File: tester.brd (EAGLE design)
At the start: 56 x 67 mm, 71 parts, among them IC1 ATmega8/88/168, K1 NA 05W K, M1 SP6000C-180, P1 250, P2 10k lin, Q1 BC847CSMD, Q2 BC847CSMD, Q3 BC807-40SMD, Q4 8,000 MHz, Q5 BC847CSMD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

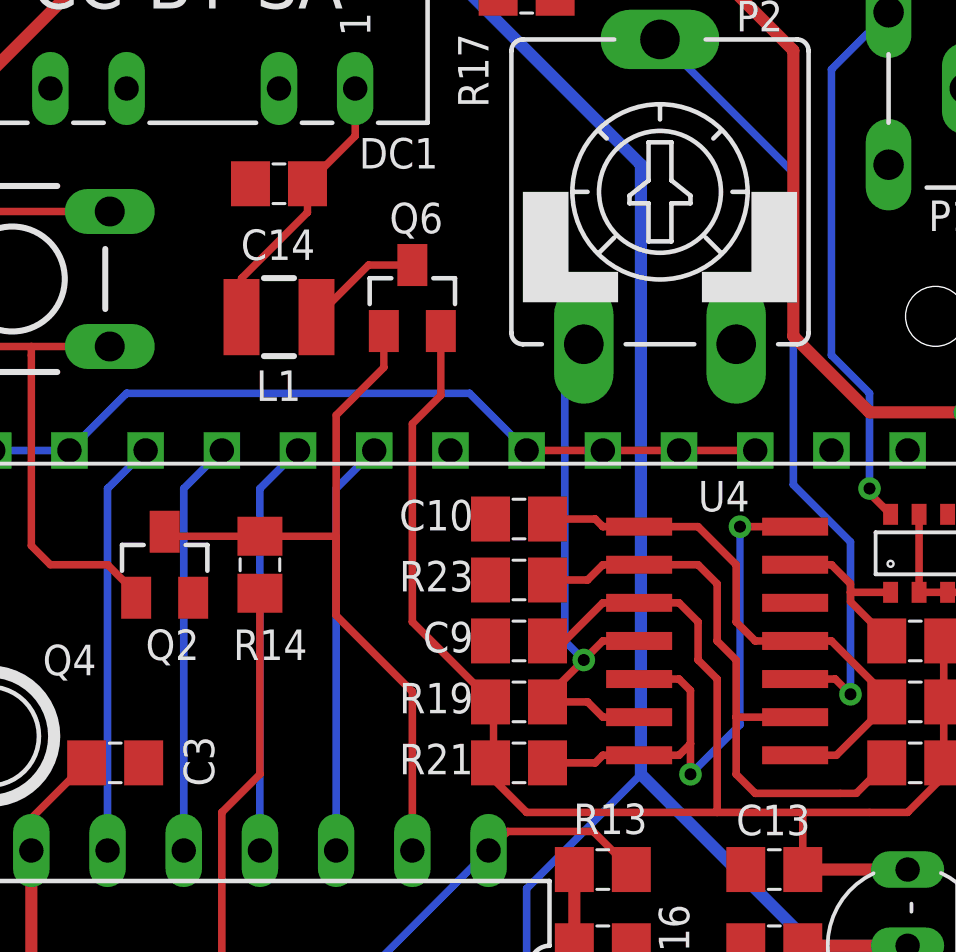
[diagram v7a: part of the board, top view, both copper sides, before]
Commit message: bigger pads for L1
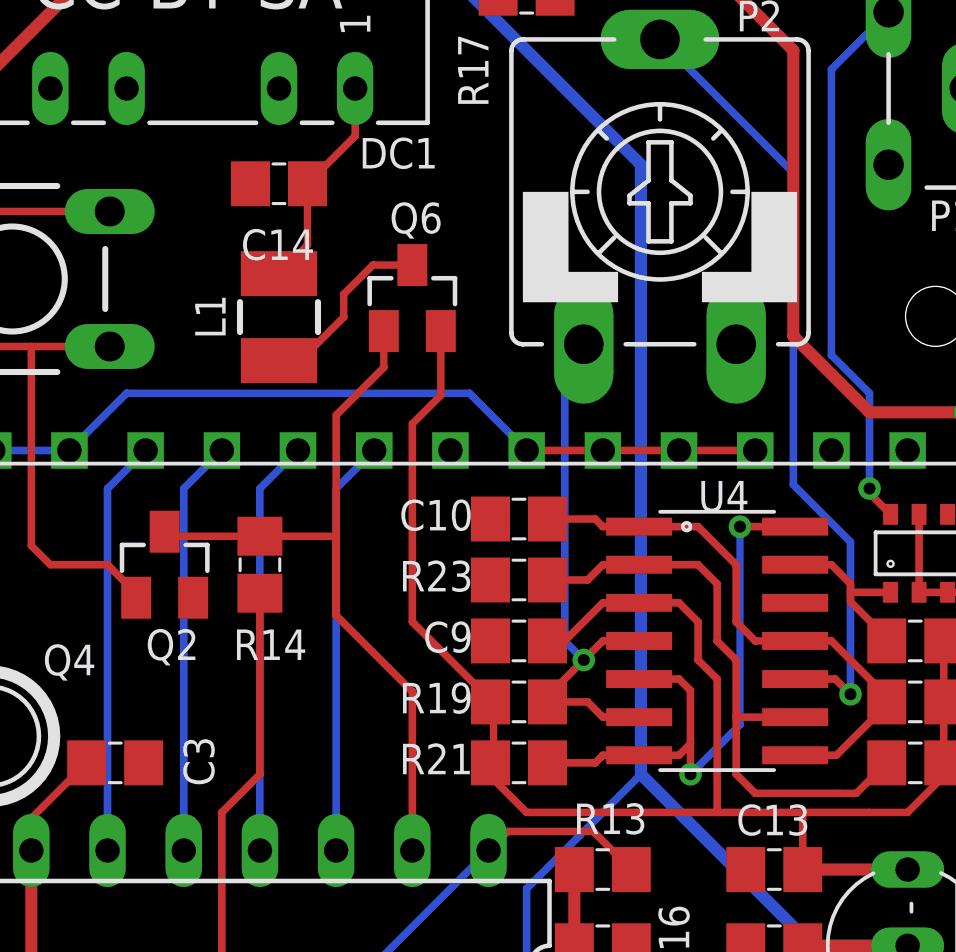
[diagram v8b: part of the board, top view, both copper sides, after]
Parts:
- L1: device inductor-neosid:SM-NE29 -> inductor-neosid:SM-NE29-B
- turned L1 to 90 degrees
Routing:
- net N$24: track 3.91 -> 6.21 mm
- net N$25: track 9.19 -> 7.22 mm
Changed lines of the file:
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@@
 <setting verticaltext="up"/>
 </settings>
-<grid distance="0.635" unitdist="mm" unit="mm" style="lines" multiple="1" display="yes" altdistance="5" altunitdist="mil" altunit="mic"/>
+<grid distance="0.635" unitdist="mm" unit="mm" style="lines" multiple="1" display="yes" altdistance="0.127" altunitdist="mm" altunit="mm"/>
 <layers>
 <layer number="1" name="Top" color="4" fill="1" visible="yes" active="yes"/>
@@
 <attribute name="VALUE" x="8.12" y="57.07" size="1.27" layer="27"/>
 </element>
-<element name="L1" library="inductor-neosid" package="SM-NE29" value="33u" x="31.115" y="53.975" smashed="yes" rot="R180">
-<attribute name="NAME" x="30.353" y="51.181" size="1.016" layer="25"/>
-<attribute name="VALUE" x="36.405" y="56.535" size="1.27" layer="27" rot="R180"/>
-<attribute name="OC_NEWARK" value="unknown" x="31.115" y="53.975" size="1.778" layer="27" rot="R180" display="off"/>
-<attribute name="MPN" value="" x="31.115" y="53.975" size="1.778" layer="27" rot="R180" display="off"/>
-<attribute name="MF" value="" x="31.115" y="53.975" size="1.778" layer="27" rot="R180" display="off"/>
-<attribute name="OC_FARNELL" value="unknown" x="31.115" y="53.975" size="1.778" layer="27" rot="R180" display="off"/>
+<element name="L1" library="inductor-neosid" package="SM-NE29-B" value="33u" x="31.115" y="53.975" smashed="yes" rot="R90">
+<attribute name="NAME" x="28.321" y="54.737" size="1.016" layer="25" rot="R270"/>
+<attribute name="VALUE" x="33.675" y="48.685" size="1.27" layer="27" rot="R90"/>
 </element>
 <element name="C7" library="rcl" package="C0805" value="1u" x="8.89" y="40.64" smashed="yes" rot="R270">
@@
 <contactref element="L1" pad="1"/>
 <contactref element="Q6" pad="3"/>
-<wire x1="35.56" y1="55.71" x2="34.1" y2="55.71" width="0.25" layer="1"/>
-<wire x1="34.1" y1="55.71" x2="32.365" y2="53.975" width="0.25" layer="1"/>
+<wire x1="31.115" y1="52.525" x2="31.824" y2="52.525" width="0.25" layer="1"/>
+<wire x1="31.824" y1="52.525" x2="33.274" y2="53.975" width="0.25" layer="1"/>
+<wire x1="33.274" y1="53.975" x2="33.274" y2="54.737" width="0.25" layer="1"/>
+<wire x1="33.274" y1="54.737" x2="34.247" y2="55.71" width="0.25" layer="1"/>
+<wire x1="34.247" y1="55.71" x2="35.56" y2="55.71" width="0.25" layer="1"/>
 </signal>
 <signal name="N$25">
@@
 <contactref element="DC1" pad="1"/>
 <contactref element="L1" pad="2"/>
-<wire x1="29.865" y1="53.975" x2="29.865" y2="55.265" width="0.25" layer="1"/>
-<wire x1="29.865" y1="55.265" x2="32.065" y2="57.465" width="0.25" layer="1"/>
-<wire x1="32.065" y1="57.465" x2="32.065" y2="58.42" width="0.25" layer="1"/>
 <wire x1="32.065" y1="58.42" x2="33.655" y2="60.01" width="0.25" layer="1"/>
 <wire x1="33.655" y1="60.01" x2="33.655" y2="61.595" width="0.25" layer="1"/>
+<wire x1="32.065" y1="58.42" x2="32.065" y2="56.375" width="0.25" layer="1"/>
+<wire x1="32.065" y1="56.375" x2="31.115" y2="55.425" width="0.25" layer="1"/>
 </signal>
 <signal name="N$28">
